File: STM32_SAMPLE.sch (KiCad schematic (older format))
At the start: 41 parts, among them J1 USB_B_Micro, J2 Conn_01x03_Male, J3 Conn_01x03_Male, J4 Conn_01x05_Male, SW1 SW_Push, U1 LM1117-3.3, U2 STM32F405RGTx

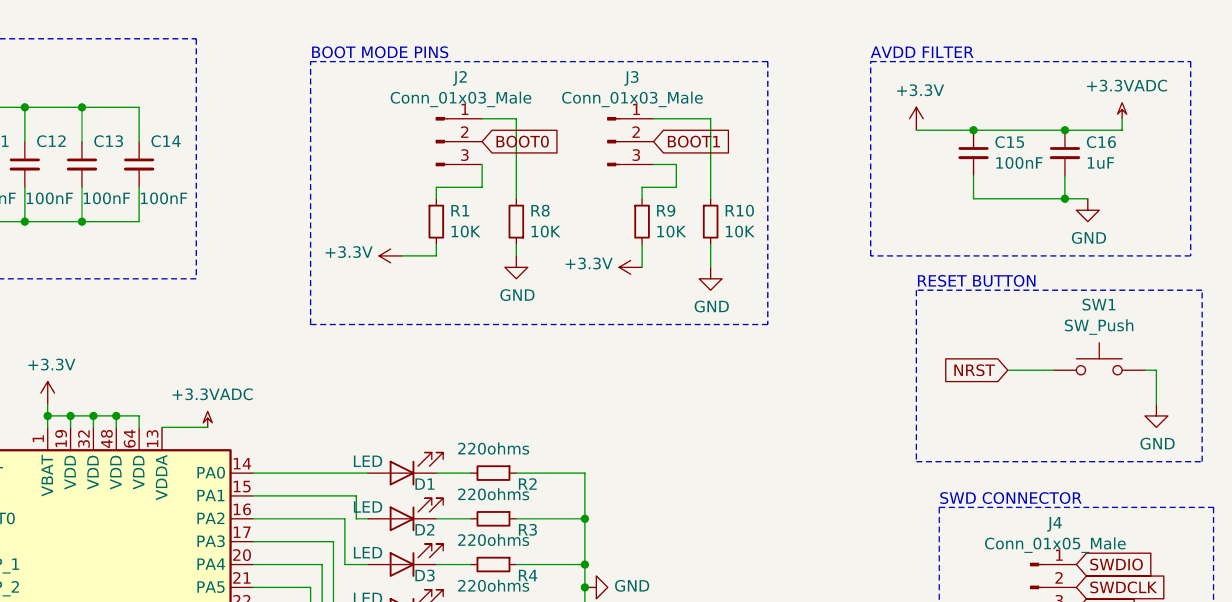
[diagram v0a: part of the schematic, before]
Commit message: updated VDDA jumper
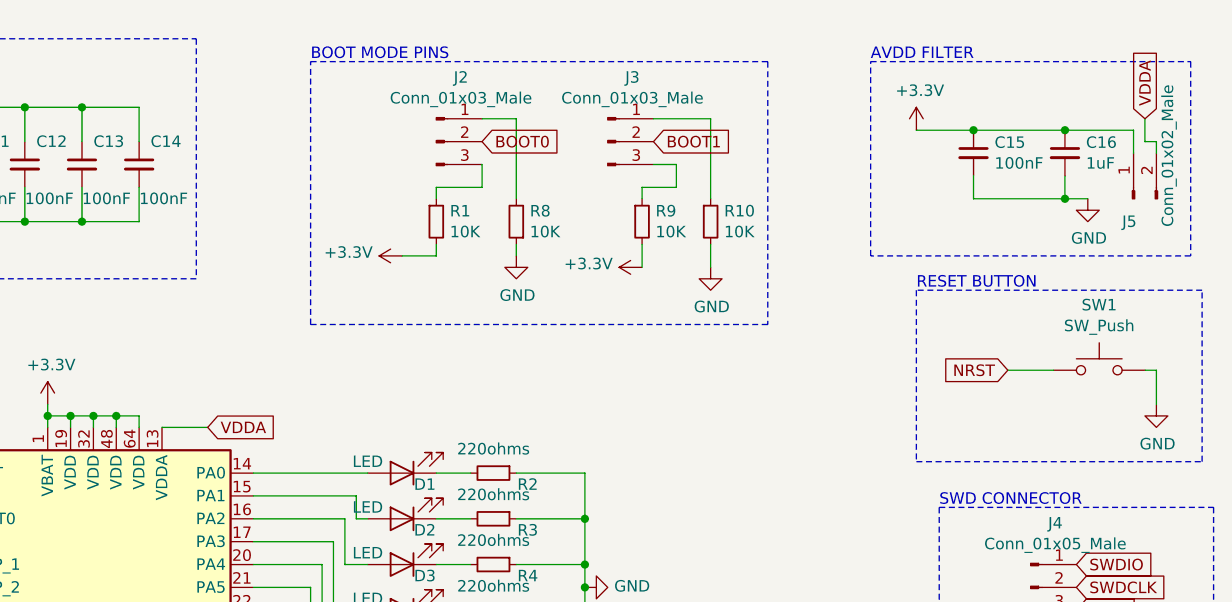
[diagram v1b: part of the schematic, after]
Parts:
- added J5: Conn_01x02_Male, Connector_PinHeader_2.54mm:PinHeader_1x02_P2.54mm_Vertical, symbol Connector:Conn_01x02_Male
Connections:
- net +3.3VADC renamed +3V3
- net +3V3: now also J5.1 (Pin_1); no longer U2.13 (VDDA)
- new net VDDA: J5.2 (Pin_2), U2.13 (VDDA)
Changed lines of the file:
@@
 Wire Wire Line
 	9550 1000 9800 1000
-Wire Wire Line
-	9800 1000 10200 1000
-Connection ~ 9800 1000
 $Comp
 L power:GND #PWR020
@@
 Wire Wire Line
 	10200 1300 10300 1300
-$Comp
-L power:+3.3VADC #PWR024
-U 1 1 5E94C52B
-P 10450 950
-F 0 "#PWR024" H 10600 900 50  0001 C CNN
-F 1 "+3.3VADC" H 10470 1093 50  0000 C CNN
-F 2 "" H 10450 950 50  0001 C CNN
-F 3 "" H 10450 950 50  0001 C CNN
-	1    10450 950
-	1    0    0    -1
-$EndComp
-Wire Wire Line
-	10200 1000 10450 1000
-Wire Wire Line
-	10450 1000 10450 950
-Connection ~ 10200 1000
-$Comp
-L power:+3.3VADC #PWR012
-U 1 1 5E94D744
-P 6450 2300
-F 0 "#PWR012" H 6600 2250 50  0001 C CNN
-F 1 "+3.3VADC" H 6470 2443 50  0000 C CNN
-F 2 "" H 6450 2300 50  0001 C CNN
-F 3 "" H 6450 2300 50  0001 C CNN
-	1    6450 2300
-	1    0    0    -1
-$EndComp
 Wire Wire Line
 	6250 2300 6450 2300
@@
 Wire Wire Line
 	6900 3500 7150 3500
+Text GLabel 10550 950  1    50   Input ~ 0
+VDDA
+Text GLabel 6450 2300 2    50   Input ~ 0
+VDDA
+$Comp
+L Connector:Conn_01x02_Male J5
+U 1 1 5EB1E8E0
+P 10500 1300
+F 0 "J5" V 10400 1350 50  0000 R CNN
+F 1 "Conn_01x02_Male" H 11000 1150 50  0000 R CNN
+F 2 "Connector_PinHeader_2.54mm:PinHeader_1x02_P2.54mm_Vertical" H 10500 1300 50  0001 C CNN
+F 3 "~" H 10500 1300 50  0001 C CNN
+	1    10500 1300
+	0    -1   -1   0
+$EndComp
+Wire Wire Line
+	9800 1000 10200 1000
+Connection ~ 9800 1000
+Wire Wire Line
+	10500 1000 10500 1100
+Wire Wire Line
+	10200 1000 10500 1000
+Connection ~ 10200 1000
+Wire Wire Line
+	10550 950  10550 1050
+Wire Wire Line
+	10550 1050 10600 1050
+Wire Wire Line
+	10600 1050 10600 1100
 $EndSCHEMATC

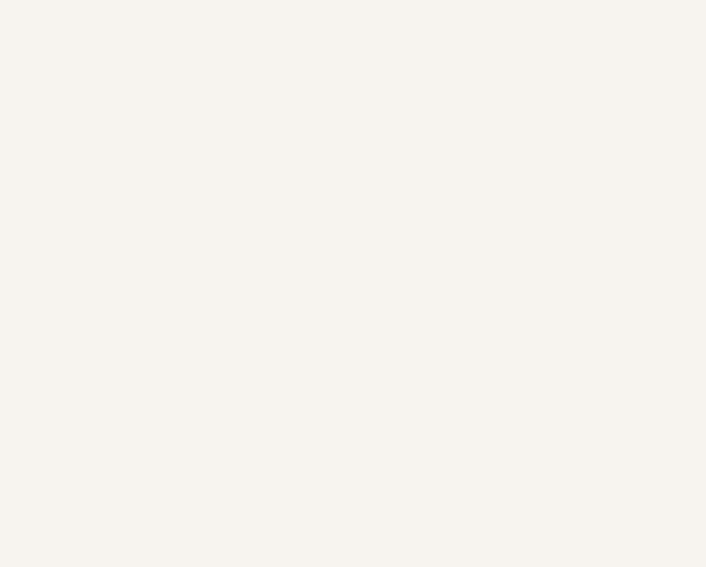
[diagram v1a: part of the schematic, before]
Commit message: grounded mounting holes
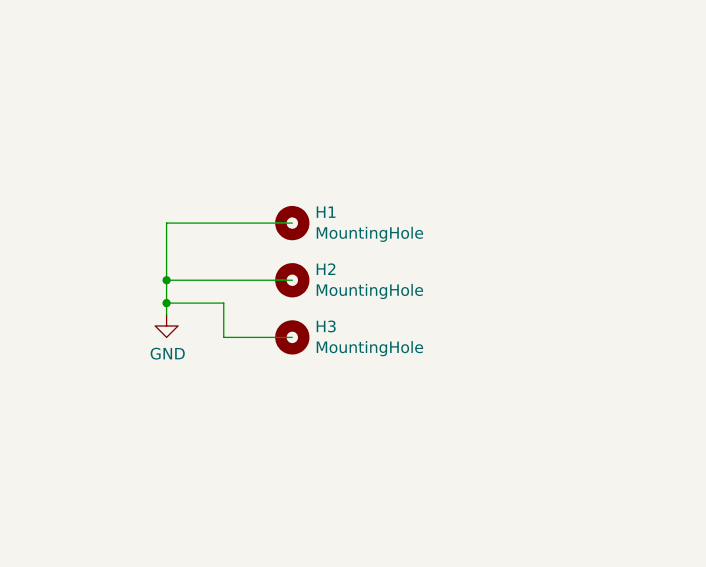
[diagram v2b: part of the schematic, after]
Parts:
- added H1, H2, H3: MountingHole, MountingHole:MountingHole_3.5mm, symbol Mechanical:MountingHole
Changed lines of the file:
@@
 EESchema Schematic File Version 4
+LIBS:STM32_SAMPLE-cache
 EELAYER 29 0
 EELAYER END
@@
 Wire Wire Line
 	10600 1050 10600 1100
+$Comp
+L Mechanical:MountingHole H1
+U 1 1 5E94E8B0
+P 1950 3400
+F 0 "H1" H 2050 3446 50  0000 L CNN
+F 1 "MountingHole" H 2050 3355 50  0000 L CNN
+F 2 "MountingHole:MountingHole_3.5mm" H 1950 3400 50  0001 C CNN
+F 3 "~" H 1950 3400 50  0001 C CNN
+	1    1950 3400
+	1    0    0    -1
+$EndComp
+$Comp
+L Mechanical:MountingHole H2
+U 1 1 5E94ECAC
+P 1950 3650
+F 0 "H2" H 2050 3696 50  0000 L CNN
+F 1 "MountingHole" H 2050 3605 50  0000 L CNN
+F 2 "MountingHole:MountingHole_3.5mm" H 1950 3650 50  0001 C CNN
+F 3 "~" H 1950 3650 50  0001 C CNN
+	1    1950 3650
+	1    0    0    -1
+$EndComp
+$Comp
+L Mechanical:MountingHole H3
+U 1 1 5E94F302
+P 1950 3900
+F 0 "H3" H 2050 3946 50  0000 L CNN
+F 1 "MountingHole" H 2050 3855 50  0000 L CNN
+F 2 "MountingHole:MountingHole_3.5mm" H 1950 3900 50  0001 C CNN
+F 3 "~" H 1950 3900 50  0001 C CNN
+	1    1950 3900
+	1    0    0    -1
+$EndComp
+$Comp
+L power:GND #PWR012
+U 1 1 5E94FB07
+P 1400 3800
+F 0 "#PWR012" H 1400 3550 50  0001 C CNN
+F 1 "GND" H 1405 3627 50  0000 C CNN
+F 2 "" H 1400 3800 50  0001 C CNN
+F 3 "" H 1400 3800 50  0001 C CNN
+	1    1400 3800
+	1    0    0    -1
+$EndComp
+Wire Wire Line
+	1400 3800 1400 3750
+Wire Wire Line
+	1400 3400 1950 3400
+Wire Wire Line
+	1950 3650 1400 3650
+Connection ~ 1400 3650
+Wire Wire Line
+	1400 3650 1400 3400
+Wire Wire Line
+	1400 3750 1650 3750
+Wire Wire Line
+	1650 3750 1650 3900
+Connection ~ 1400 3750
+Wire Wire Line
+	1400 3750 1400 3650
+Wire Wire Line
+	1950 3900 1650 3900
 $EndSCHEMATC
